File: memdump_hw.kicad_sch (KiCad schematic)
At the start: 76 parts, among them J1 USB_C_USB2.0, J2 SWD, J3 LEVEL, J4 BOOT0, Q1 SI4800, SW1 RESET, U1 AMS1117-3.3, U2 STM32F103C8, U3 74HC595, U4 74HC595, U5 74HC595, U6 SST39SF040, Y1 12M

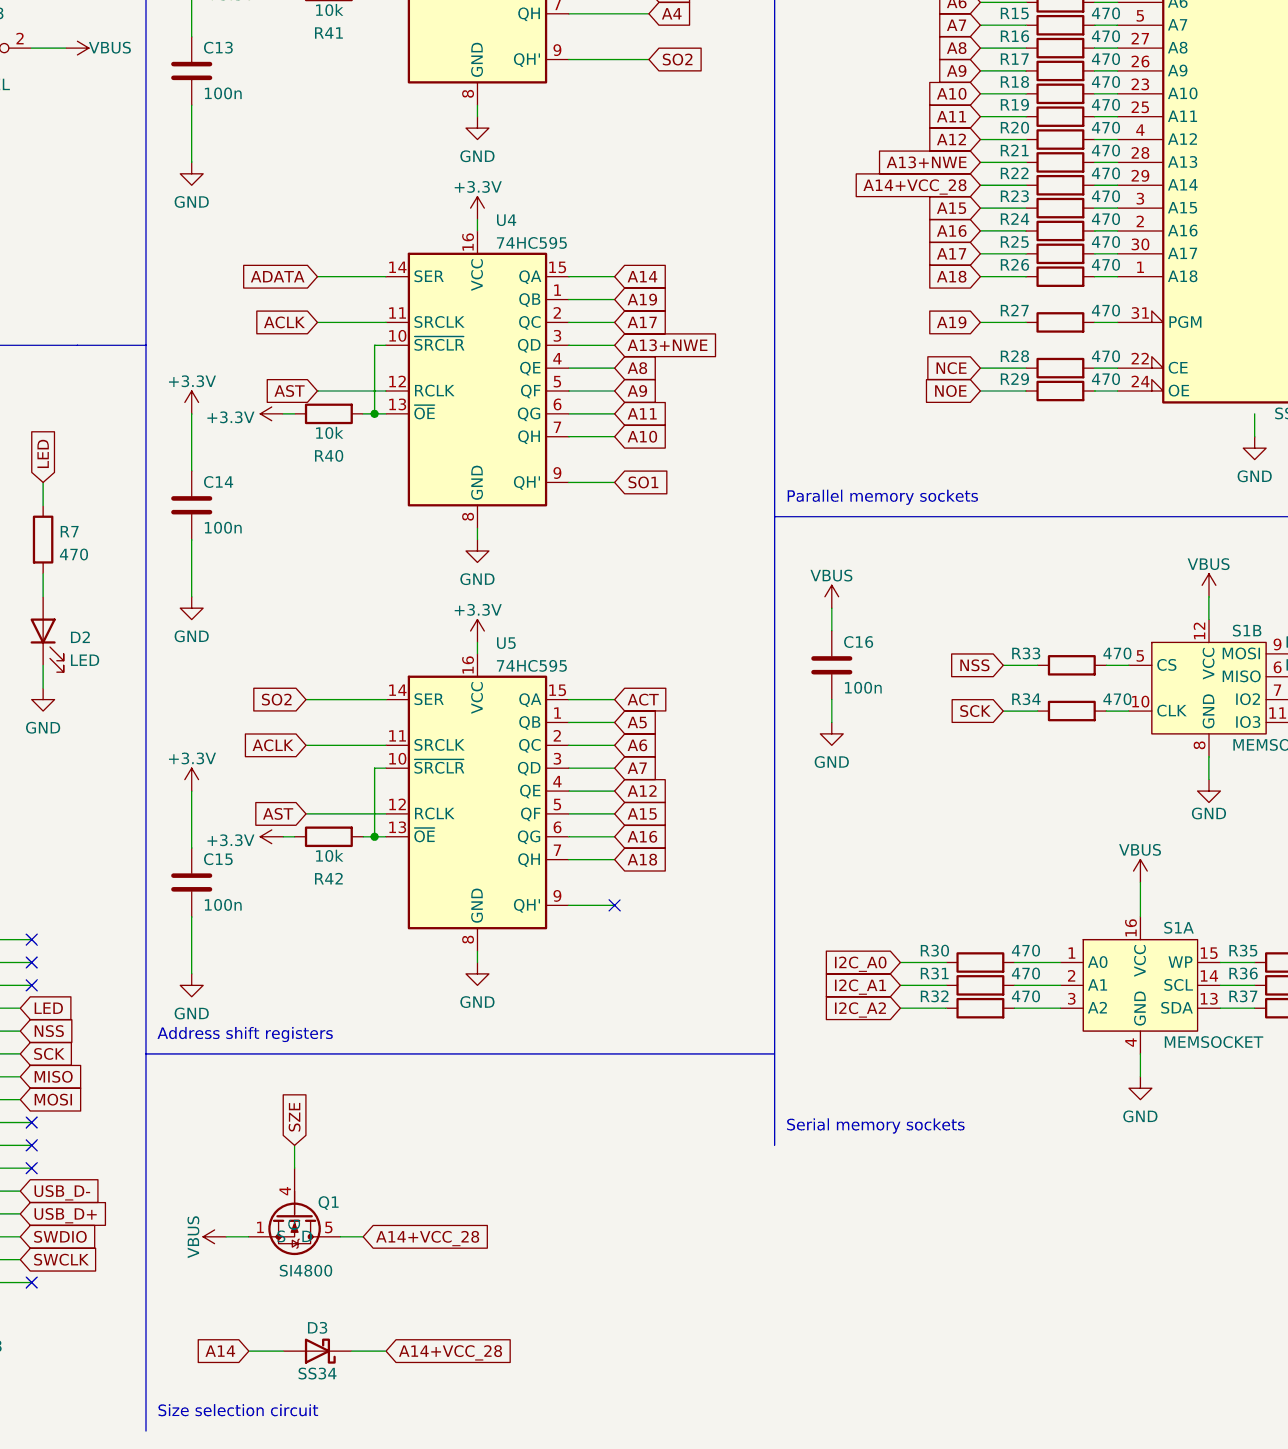
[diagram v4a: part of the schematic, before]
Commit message: fix: moved R22 to the shiftreg side of the size selection circuit
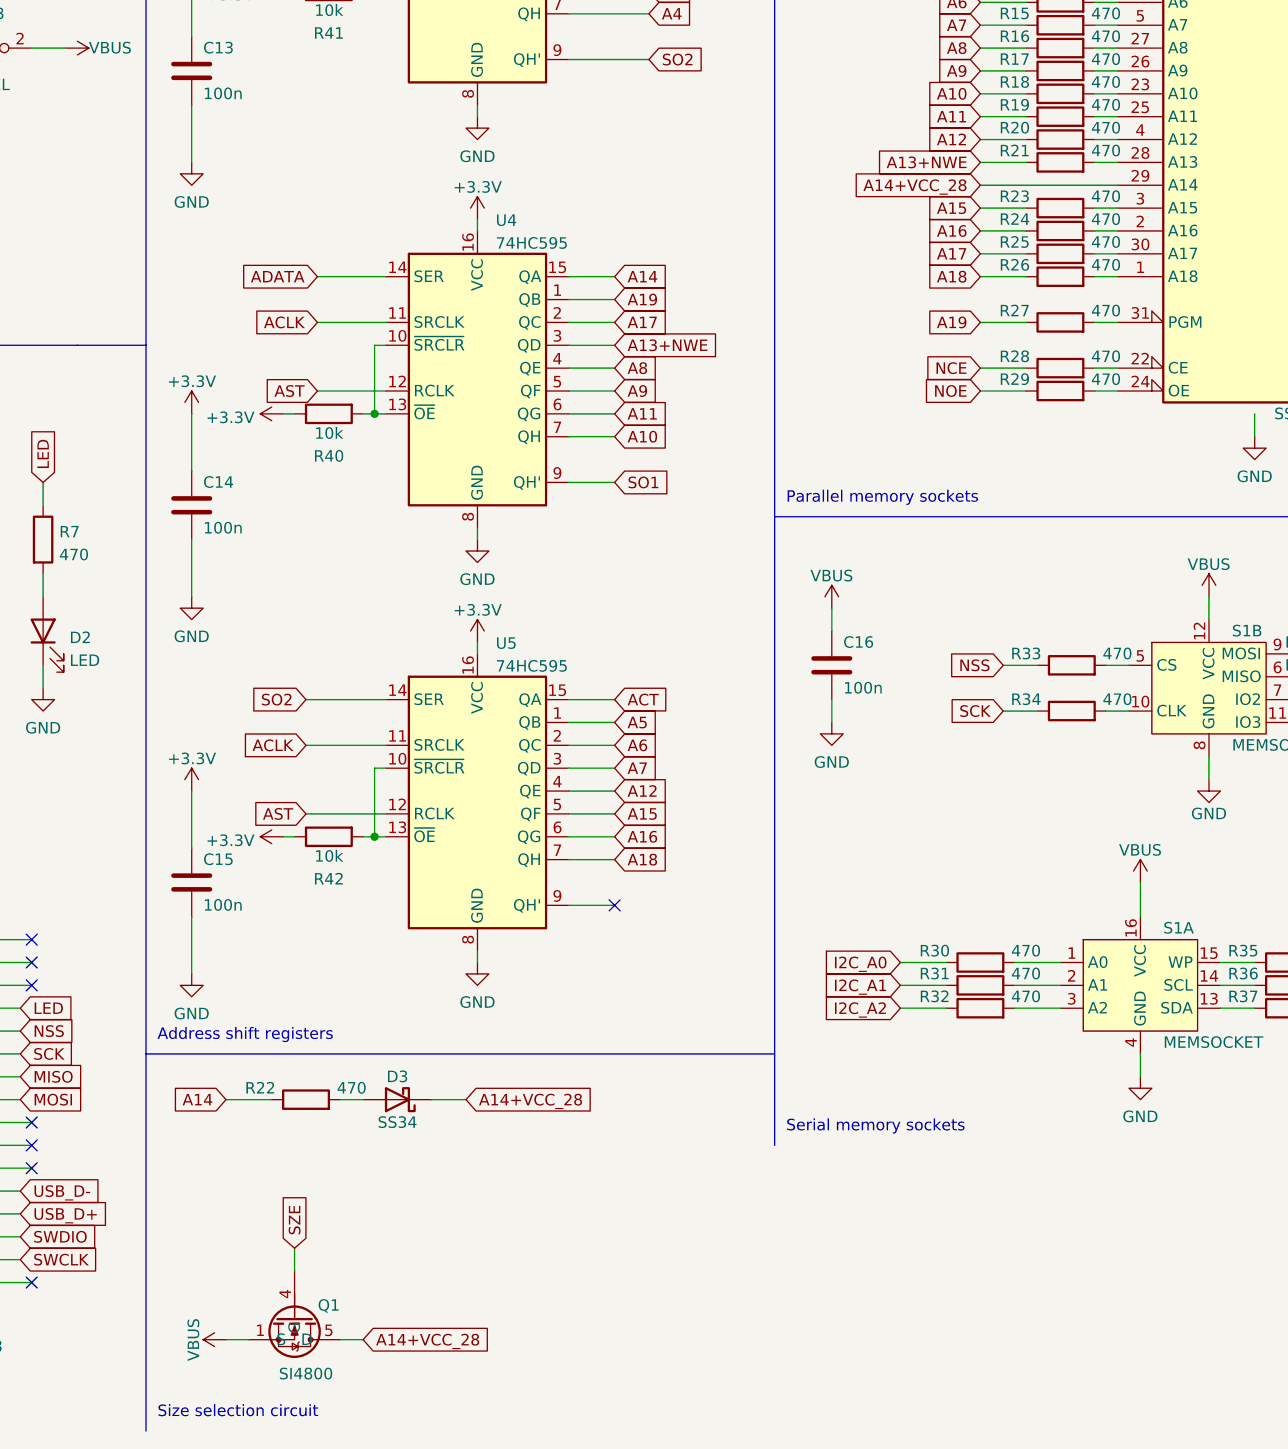
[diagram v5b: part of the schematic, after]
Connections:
- net A14: now also R22.1; no longer D3.2 (A)
- net A14+VCC_28: now also U6.29 (A14); no longer R22.1
- net at R22.2: now also D3.2 (A); no longer U6.29 (A14)
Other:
- moved on the sheet: D3, Q1, R22
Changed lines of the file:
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@@
     (stroke (width 0) (type default) (color 0 0 0 0))
   )
-  (wire (pts (xy 223.52 59.69) (xy 228.6 59.69))
+  (wire (pts (xy 223.52 59.69) (xy 238.76 59.69))
     (stroke (width 0) (type default) (color 0 0 0 0))
   )
@@
     (stroke (width 0) (type default) (color 0 0 0 0))
   )
-  (wire (pts (xy 236.22 59.69) (xy 238.76 59.69))
-    (stroke (width 0) (type default) (color 0 0 0 0))
-  )
   (wire (pts (xy 100.33 107.95) (xy 100.33 110.49))
     (stroke (width 0) (type default) (color 0 0 0 0))
@@
     (stroke (width 0) (type default) (color 0 0 0 0))
   )
-  (wire (pts (xy 152.4 176.53) (xy 154.94 176.53))
+  (wire (pts (xy 152.4 187.96) (xy 154.94 187.96))
     (stroke (width 0) (type default) (color 0 0 0 0))
   )
@@
     (stroke (width 0) (type default) (color 0 0 0 0))
   )
-  (wire (pts (xy 147.32 166.37) (xy 147.32 168.91))
+  (wire (pts (xy 147.32 177.8) (xy 147.32 180.34))
     (stroke (width 0) (type default) (color 0 0 0 0))
   )
@@
     (stroke (width 0) (type default) (color 0 0 0 0))
   )
-  (wire (pts (xy 153.67 189.23) (xy 157.48 189.23))
+  (wire (pts (xy 162.56 161.29) (xy 166.37 161.29))
     (stroke (width 0) (type default) (color 0 0 0 0))
   )
@@
     (stroke (width 0) (type default) (color 0 0 0 0))
   )
-  (wire (pts (xy 142.24 189.23) (xy 146.05 189.23))
+  (wire (pts (xy 152.4 161.29) (xy 154.94 161.29))
     (stroke (width 0) (type default) (color 0 0 0 0))
   )
@@
     (stroke (width 0) (type default) (color 0 0 0 0))
   )
-  (wire (pts (xy 139.7 176.53) (xy 142.24 176.53))
+  (wire (pts (xy 139.7 187.96) (xy 142.24 187.96))
     (stroke (width 0) (type default) (color 0 0 0 0))
   )
@@
     (stroke (width 0) (type default) (color 0 0 0 0))
   )
+  (wire (pts (xy 139.7 161.29) (xy 144.78 161.29))
+    (stroke (width 0) (type default) (color 0 0 0 0))
+  )
   (wire (pts (xy 135.89 140.97) (xy 135.89 147.32))
     (stroke (width 0) (type default) (color 0 0 0 0))
@@
     )
   )
-  (global_label "A14+VCC_28" (shape input) (at 154.94 176.53 0) (fields_autoplaced)
+  (global_label "A14+VCC_28" (shape input) (at 154.94 187.96 0) (fields_autoplaced)
     (effects (font (size 1.27 1.27)) (justify left))
-    (property "Intersheet References" "${INTERSHEET_REFS}" (id 0) (at 169.4483 176.4506 0)
+    (property "Intersheet References" "${INTERSHEET_REFS}" (id 0) (at 169.4483 187.8806 0)
       (effects (font (size 1.27 1.27)) (justify left) hide)
     )
@@
     )
   )
-  (global_label "A14+VCC_28" (shape input) (at 157.48 189.23 0) (fields_autoplaced)
+  (global_label "A14+VCC_28" (shape input) (at 166.37 161.29 0) (fields_autoplaced)
     (effects (font (size 1.27 1.27)) (justify left))
-    (property "Intersheet References" "${INTERSHEET_REFS}" (id 0) (at 171.9883 189.1506 0)
+    (property "Intersheet References" "${INTERSHEET_REFS}" (id 0) (at 180.8783 161.2106 0)
       (effects (font (size 1.27 1.27)) (justify left) hide)
     )
@@
     )
   )
-  (global_label "A14" (shape input) (at 142.24 189.23 180) (fields_autoplaced)
+  (global_label "A14" (shape input) (at 139.7 161.29 180) (fields_autoplaced)
     (effects (font (size 1.27 1.27)) (justify right))
-    (property "Intersheet References" "${INTERSHEET_REFS}" (id 0) (at 136.3193 189.1506 0)
+    (property "Intersheet References" "${INTERSHEET_REFS}" (id 0) (at 133.7793 161.2106 0)
       (effects (font (size 1.27 1.27)) (justify right) hide)
     )
@@
     )
   )
-  (global_label "SZE" (shape input) (at 147.32 166.37 90) (fields_autoplaced)
+  (global_label "SZE" (shape input) (at 147.32 177.8 90) (fields_autoplaced)
     (effects (font (size 1.27 1.27)) (justify left))
-    (property "Intersheet References" "${INTERSHEET_REFS}" (id 0) (at 147.2406 160.3888 90)
+    (property "Intersheet References" "${INTERSHEET_REFS}" (id 0) (at 147.2406 171.8188 90)
       (effects (font (size 1.27 1.27)) (justify right) hide)
     )
@@
     (pin "1")
   )
-  (symbol (lib_id "memdump:SI4800") (at 147.32 176.53 270) (unit 1)
+  (symbol (lib_id "memdump:SI4800") (at 147.32 187.96 270) (unit 1)
     (in_bom yes) (on_board yes)
-    (property "Reference" "Q1" (id 0) (at 151.13 172.72 90))
-    (property "Value" "SI4800" (id 1) (at 148.59 180.34 90))
-    (property "Footprint" "Package_SO:SO-8_3.9x4.9mm_P1.27mm" (id 2) (at 147.32 176.53 0)
+    (property "Reference" "Q1" (id 0) (at 151.13 184.15 90))
+    (property "Value" "SI4800" (id 1) (at 148.59 191.77 90))
+    (property "Footprint" "Package_SO:SO-8_3.9x4.9mm_P1.27mm" (id 2) (at 147.32 187.96 0)
       (effects (font (size 1.27 1.27)) hide)
     )
-    (property "Datasheet" "" (id 3) (at 147.32 176.53 0)
+    (property "Datasheet" "" (id 3) (at 147.32 187.96 0)
       (effects (font (size 1.27 1.27)) hide)
     )
@@
     (pin "1")
   )
-  (symbol (lib_id "Device:R") (at 232.41 59.69 90) (unit 1)
+  (symbol (lib_id "Device:R") (at 148.59 161.29 90) (unit 1)
     (in_bom yes) (on_board yes)
-    (property "Reference" "R22" (id 0) (at 227.33 58.42 90))
-    (property "Value" "470" (id 1) (at 237.49 58.42 90))
-    (property "Footprint" "Resistor_SMD:R_0805_2012Metric_Pad1.20x1.40mm_HandSolder" (id 2) (at 232.41 61.468 90)
+    (property "Reference" "R22" (id 0) (at 143.51 160.02 90))
+    (property "Value" "470" (id 1) (at 153.67 160.02 90))
+    (property "Footprint" "Resistor_SMD:R_0805_2012Metric_Pad1.20x1.40mm_HandSolder" (id 2) (at 148.59 163.068 90)
       (effects (font (size 1.27 1.27)) hide)
     )
-    (property "Datasheet" "~" (id 3) (at 232.41 59.69 0)
+    (property "Datasheet" "~" (id 3) (at 148.59 161.29 0)
       (effects (font (size 1.27 1.27)) hide)
     )
@@
     (pin "2")
   )
-  (symbol (lib_id "Device:D_Schottky") (at 149.86 189.23 180) (unit 1)
+  (symbol (lib_id "Device:D_Schottky") (at 158.75 161.29 180) (unit 1)
     (in_bom yes) (on_board yes)
-    (property "Reference" "D3" (id 0) (at 149.86 186.69 0))
-    (property "Value" "SS34" (id 1) (at 149.86 191.77 0))
-    (property "Footprint" "Diode_SMD:D_1206_3216Metric_Pad1.42x1.75mm_HandSolder" (id 2) (at 149.86 189.23 0)
+    (property "Reference" "D3" (id 0) (at 158.75 158.75 0))
+    (property "Value" "SS34" (id 1) (at 158.75 163.83 0))
+    (property "Footprint" "Diode_SMD:D_1206_3216Metric_Pad1.42x1.75mm_HandSolder" (id 2) (at 158.75 161.29 0)
       (effects (font (size 1.27 1.27)) hide)
     )
-    (property "Datasheet" "~" (id 3) (at 149.86 189.23 0)
+    (property "Datasheet" "~" (id 3) (at 158.75 161.29 0)
       (effects (font (size 1.27 1.27)) hide)
     )
@@
     (pin "2")
   )
-  (symbol (lib_id "power:VBUS") (at 139.7 176.53 90) (mirror x) (unit 1)
+  (symbol (lib_id "power:VBUS") (at 139.7 187.96 90) (mirror x) (unit 1)
     (in_bom yes) (on_board yes) (fields_autoplaced)
-    (property "Reference" "#PWR030" (id 0) (at 143.51 176.53 0)
+    (property "Reference" "#PWR030" (id 0) (at 143.51 187.96 0)
       (effects (font (size 1.27 1.27)) hide)
     )
-    (property "Value" "VBUS" (id 1) (at 136.1242 176.53 0))
-    (property "Footprint" "" (id 2) (at 139.7 176.53 0)
+    (property "Value" "VBUS" (id 1) (at 136.1242 187.96 0))
+    (property "Footprint" "" (id 2) (at 139.7 187.96 0)
       (effects (font (size 1.27 1.27)) hide)
     )
-    (property "Datasheet" "" (id 3) (at 139.7 176.53 0)
+    (property "Datasheet" "" (id 3) (at 139.7 187.96 0)
       (effects (font (size 1.27 1.27)) hide)
     )

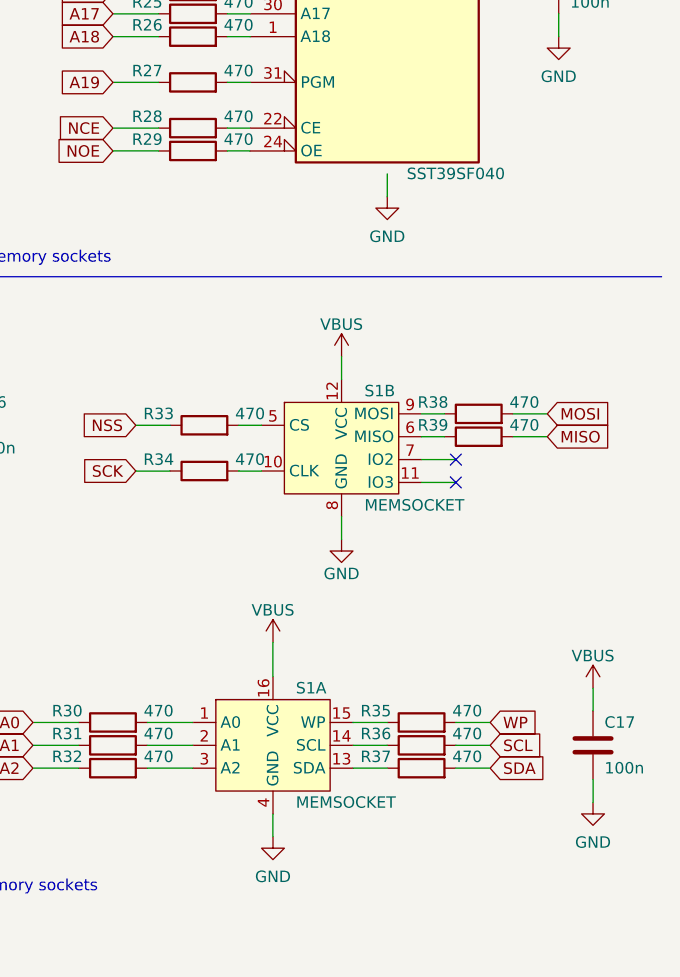
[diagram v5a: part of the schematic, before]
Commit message: fix: minor cleanup fix: branching from vias when possible fix: values moved to the respective silkscreens
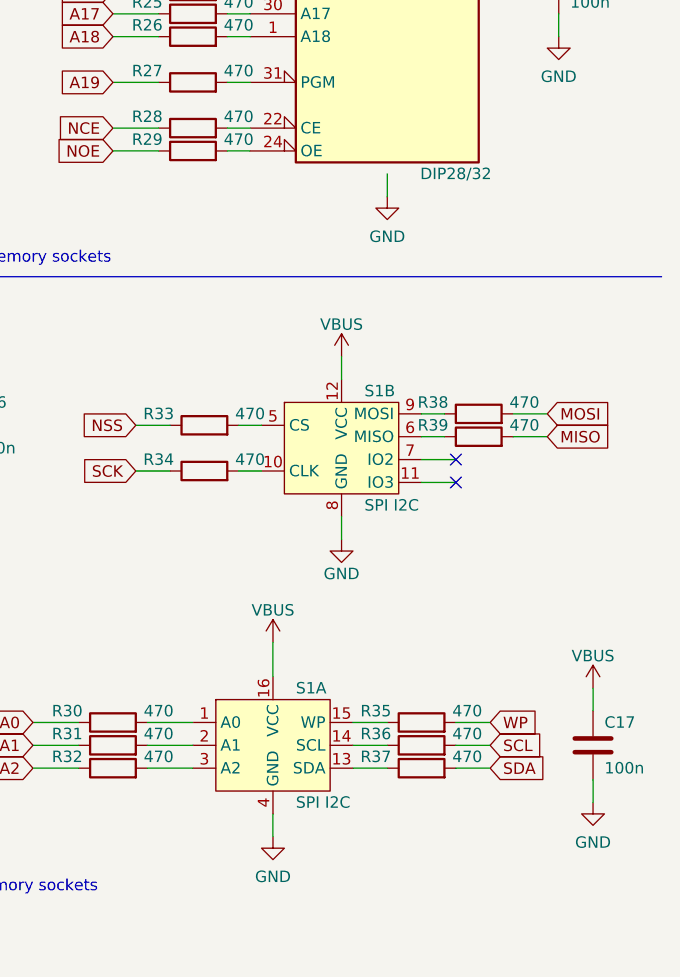
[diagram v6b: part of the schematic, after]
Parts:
- S1: value MEMSOCKET -> SPI I2C
- U6: value SST39SF040 -> DIP28/32
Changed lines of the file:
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@@
       (effects (font (size 1.27 1.27)) (justify left))
     )
-    (property "Value" "MEMSOCKET" (id 1) (at 251.46 121.92 0)
+    (property "Value" "SPI I2C" (id 1) (at 251.46 121.92 0)
       (effects (font (size 1.27 1.27)) (justify left))
     )
@@
       (effects (font (size 1.27 1.27)) (justify left))
     )
-    (property "Value" "MEMSOCKET" (id 1) (at 243.84 154.94 0)
+    (property "Value" "SPI I2C" (id 1) (at 243.84 154.94 0)
       (effects (font (size 1.27 1.27)) (justify left))
     )
@@
     (in_bom yes) (on_board yes)
     (property "Reference" "U6" (id 0) (at 260.35 21.59 0))
-    (property "Value" "SST39SF040" (id 1) (at 261.62 85.09 0))
+    (property "Value" "DIP28/32" (id 1) (at 261.62 85.09 0))
     (property "Footprint" "Socket:DIP_Socket-32_W11.9_W12.7_W15.24_W17.78_W18.5_3M_232-1285-00-0602J" (id 2) (at 254 46.99 0)
       (effects (font (size 1.27 1.27)) hide)
@@
     )
     (path "/3e22c9d2-3dbc-4c3d-b98c-2f51c5f67b31"
-      (reference "S1") (unit 1) (value "MEMSOCKET") (footprint "Socket:DIP_Socket-16_W4.3_W5.08_W7.62_W10.16_W10.9_3M_216-3340-00-0602J")
+      (reference "S1") (unit 1) (value "SPI I2C") (footprint "Socket:DIP_Socket-16_W4.3_W5.08_W7.62_W10.16_W10.9_3M_216-3340-00-0602J")
     )
     (path "/23b9a9f4-6451-4c83-a048-f7037e88c31b"
-      (reference "S1") (unit 2) (value "MEMSOCKET") (footprint "Socket:DIP_Socket-16_W4.3_W5.08_W7.62_W10.16_W10.9_3M_216-3340-00-0602J")
+      (reference "S1") (unit 2) (value "SPI I2C") (footprint "Socket:DIP_Socket-16_W4.3_W5.08_W7.62_W10.16_W10.9_3M_216-3340-00-0602J")
     )
     (path "/560c52e9-bce4-4b9e-99ae-f5412b8463f5"
@@
     )
     (path "/43d79bdd-1c63-4dc1-a6e0-61810ad9063c"
-      (reference "U6") (unit 1) (value "SST39SF040") (footprint "Socket:DIP_Socket-32_W11.9_W12.7_W15.24_W17.78_W18.5_3M_232-1285-00-0602J")
+      (reference "U6") (unit 1) (value "DIP28/32") (footprint "Socket:DIP_Socket-32_W11.9_W12.7_W15.24_W17.78_W18.5_3M_232-1285-00-0602J")
     )
     (path "/057877ef-03b8-4212-bb91-55fd22a09fa5"

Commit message: fix: USB-C to UFP
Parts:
- added D4: LED, LED_SMD:LED_0805_2012Metric_Pad1.15x1.40mm_HandSolder, symbol Device:LED
- added R12: 470, Resistor_SMD:R_0805_2012Metric_Pad1.20x1.40mm_HandSolder, symbol Device:R
- renumbered C11 to C10, C12 to C11, C13 to C12, C14 to C13, C15 to C14, C16 to C15, C18 to C16, C3 to C2, C4 to C3, C5 to C4, C6 to C5, C7 to C6, C8 to C7, C2 to C8, C10 to C9, J4 to J3, J3 to J4, R40 to R10, R42 to R11, R30 to R13, R31 to R14, R32 to R15, R8 to R16, R9 to R17, R10 to R18, R11 to R19, R12 to R20, R13 to R21, R14 to R22, R15 to R23, R16 to R24, R17 to R25, R18 to R26, R19 to R27, R20 to R28, R21 to R29, R25 to R30, R23 to R31, R24 to R32, R26 to R33, R27 to R34, R28 to R35, R29 to R36, R33 to R37, R34 to R38, R35 to R39, R36 to R40, R37 to R41, R38 to R42, R39 to R43, R22 to R8, R41 to R9
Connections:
- net +5V: no longer R3.1
- net A14: now also R30.1, U4.2 (QC); no longer R8.1, U4.15 (QA)
- net A17: now also R8.1, U4.15 (QA); no longer R30.1, U4.2 (QC)
- net ACT: now also R12.1
- net GND: now also R3.2, D4.1 (K)
- net at R30.2: now also U6.29 (A14); no longer U6.30 (A17)
- net at J1.A5 (CC1), J1.B5 (CC2): now also R3.1; no longer R3.2
- net A13+NWE renamed A13
- net A14+VCC_28 renamed A17+VCC_28
- net A17+VCC_28: now also U6.30 (A17); no longer U6.29 (A14)
- new net: D4.2 (A), R12.2
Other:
- moved on the sheet: R3, R30, R4
